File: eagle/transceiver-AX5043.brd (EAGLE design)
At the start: 40 x 35 mm, 43 parts, among them J1 142-0701-851, J2 142-0701-851, J3 142-0701-851, U1 U-ONSEMI-AX5043, U2 LP2985XX-N, X1 TAITIEN-TY

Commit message: Update layout AX5043
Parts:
- R7: device oresat-rcl:.0603-B-NOSILK -> oresat-rcl:.0603-C-NOSILK
- moved D1 63.5 mm to (4.50, 23.9), turned to 90 degrees
- moved C15 50.9 mm to (23.2, 19.3)
- moved C13 50.3 mm to (23.2, 17.1)
- moved C10 49.7 mm to (17.1, 21.9), turned to 270 degrees
- moved C14 48.1 mm to (23.2, 18.2)
- moved C16 45.3 mm to (12.1, 25.4), turned to 90 degrees
- moved C11 41.4 mm to (17.1, 24.1), turned to 90 degrees
- moved R6 39.7 mm to (6.10, 23.9), turned to 270 degrees
- moved C17 39.2 mm to (17.1, 26.8), turned to 270 degrees
- moved C12 35.4 mm to (18.2, 24.1), turned to 90 degrees
- moved R7 30.6 mm to (14.9, 29.0)
- moved JP3 8.47 mm to (31.5, 20.8)
- moved R9 6.31 mm to (19.9, 20.8)
- moved C9 5.80 mm to (12.9, 21.9), turned to 270 degrees
- moved R8 4.45 mm to (21.6, 20.8), turned to 180 degrees
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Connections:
- net N$14: now also JP3.2; no longer JP3.1
- net N$15: now also JP3.1; no longer JP3.2
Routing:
- net 2V7: track 0.00 -> 35.6 mm, vias 0 -> 7
- net N$4: track 0.00 -> 21.3 mm
- net GND: track 2.03 -> 20.4 mm, vias 0 -> 205
- net N$14: track 0.00 -> 17.2 mm, vias 0 -> 1
- net N$5: track 0.00 -> 17.0 mm
- net N$9: track 0.00 -> 16.5 mm
- net N$10: track 0.00 -> 15.8 mm
- net N$7: track 0.00 -> 15.5 mm
- net N$23: track 0.00 -> 15.3 mm
- net N$11: track 0.00 -> 15.0 mm
- net N$8: track 0.00 -> 14.9 mm
- net N$13: track 0.00 -> 14.9 mm
- net N$15: track 0.00 -> 14.2 mm, vias 0 -> 1
- net N$12: track 0.00 -> 14.1 mm
- net 1V8: track 0.00 -> 7.45 mm, vias 0 -> 2
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- added copper zone on layer 1, net 1V8
- added copper zone on layer 1, net 2V7
- added copper zone on layer 1, net N$2
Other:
- outline, holes or cut-outs redrawn

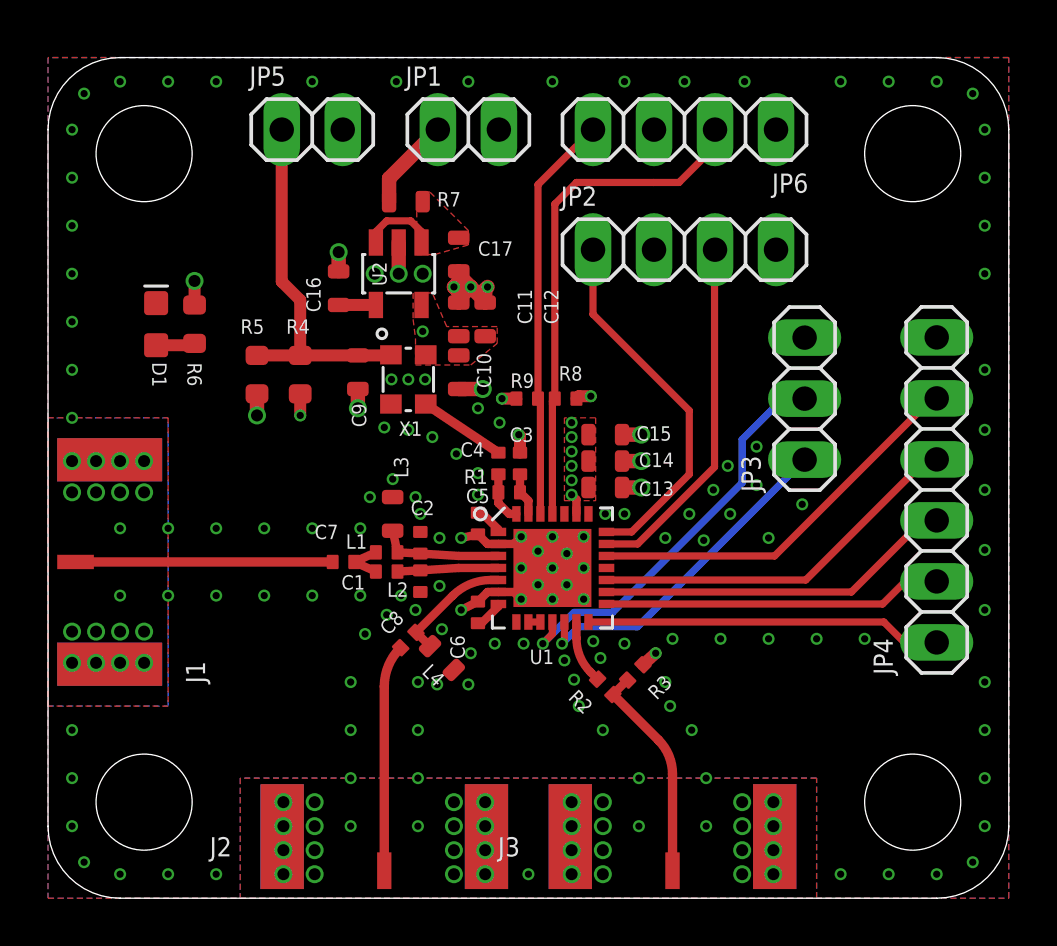
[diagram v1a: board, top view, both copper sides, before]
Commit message: Finalized AX5043 layout
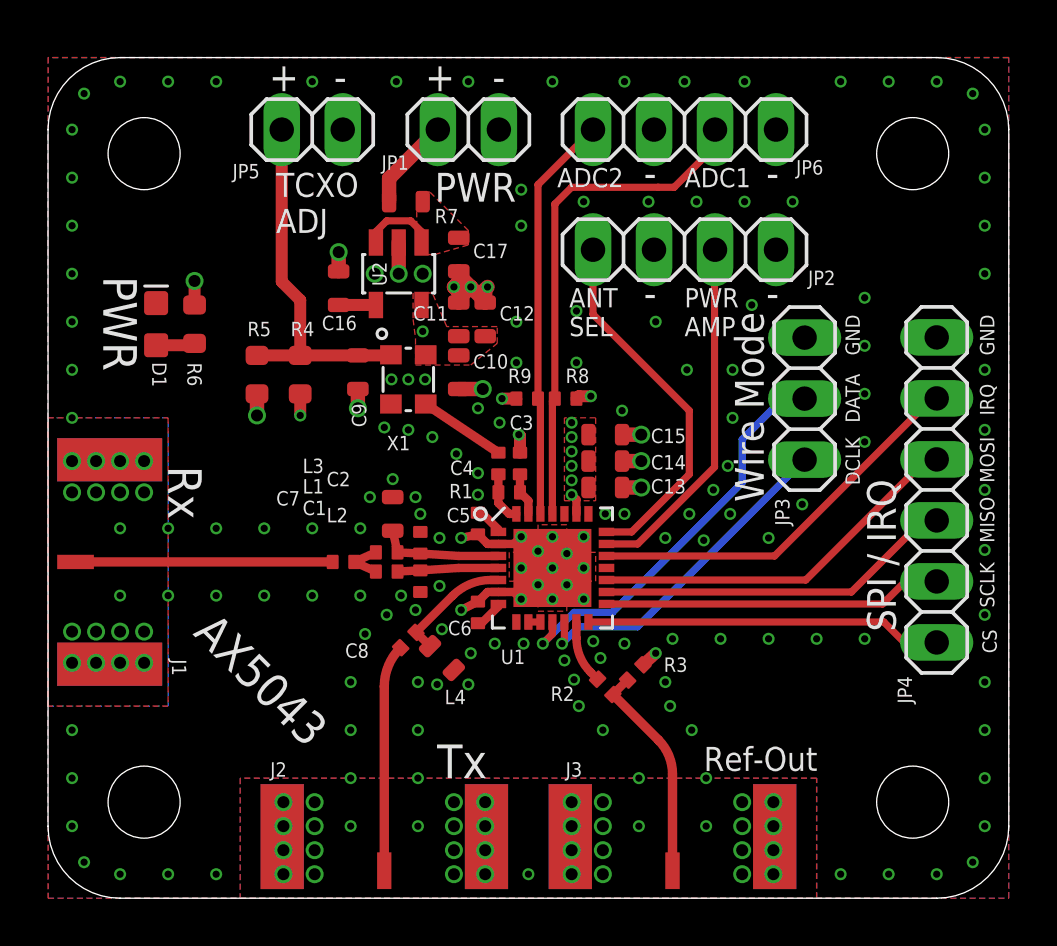
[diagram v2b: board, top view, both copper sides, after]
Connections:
- net N$10 renamed MOSI
- net N$11 renamed MISO
- net N$12 renamed SCLK
- net N$13 renamed CS
- net N$14 renamed DATA
- net N$15 renamed DCLK
- net N$4 renamed ADC1
- net N$5 renamed ADC2
- net N$7 renamed ANTSEL
- net N$8 renamed PWRAMP
- net N$9 renamed IRQ
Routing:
- net GND: vias 205 -> 224
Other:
- board text added: "+"
- board text added: "-"
- board text added: "400 - 525 MHz 800 - 1050 MHz"
- board text added: "ADC1"
- board text added: "ADC2"
- board text added: "ANT SEL"
- board text added: "AX5043"
- board text added: "CS"
- board text added: "DATA"
- board text added: "DCLK"
- board text added: "GND"
- board text added: "IRQ"
- board text added: "MISO"
- board text added: "MOSI"
- board text added: "PWR"
- board text added: "PWR AMP"
- board text added: "Ref-Out"
- board text added: "Rx"
- board text added: "SCLK"
- board text added: "SPI / IRQ"
- board text added: "TCXO ADJ"
- board text added: "Transceiver - AX5043 PSAS / OreSat 2019-10-18 v1.0 E.M. KJ7AOG"
- board text added: "Tx"
- board text added: "Wire Mode"

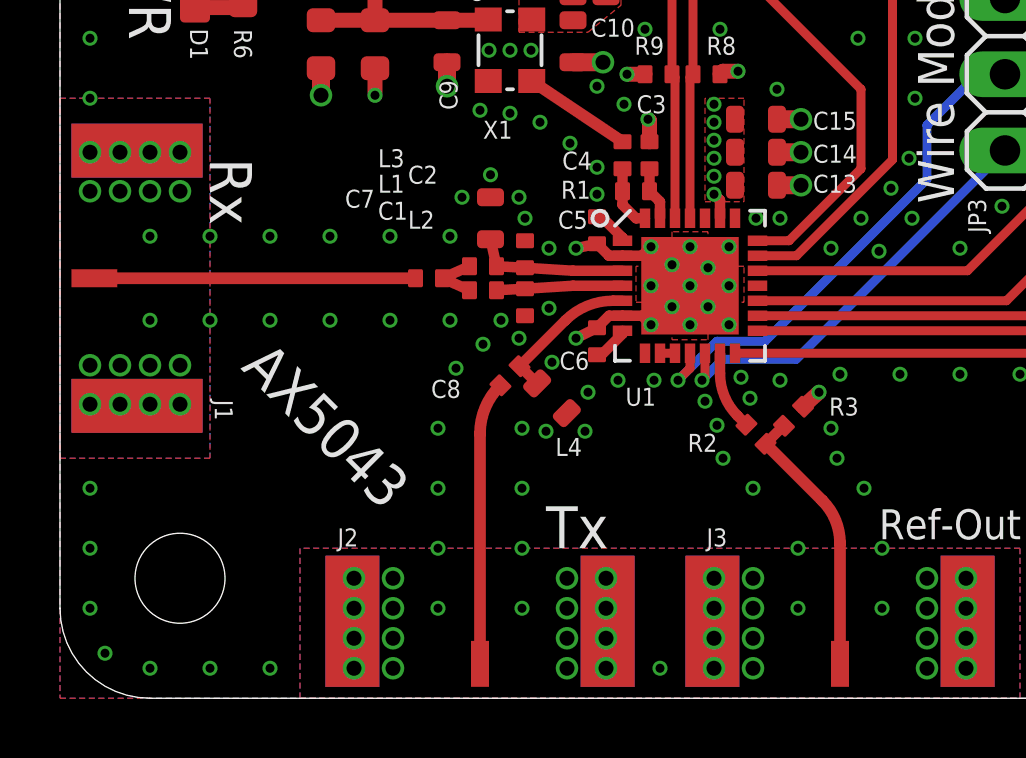
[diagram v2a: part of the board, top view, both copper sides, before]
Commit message: Update AX5043
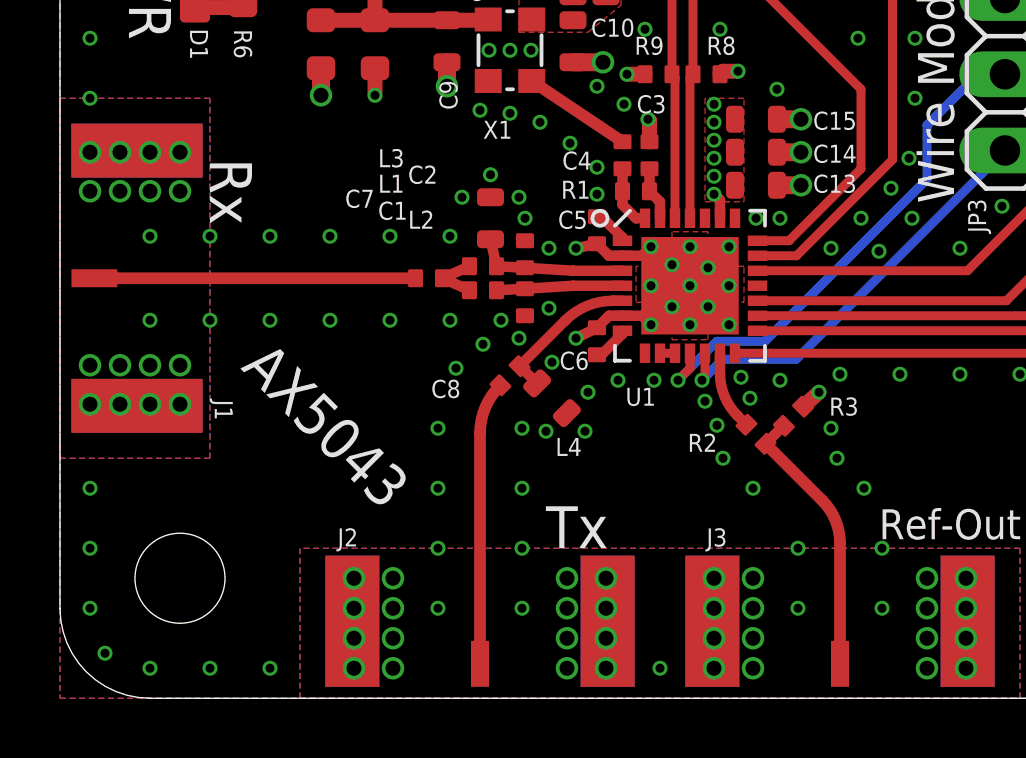
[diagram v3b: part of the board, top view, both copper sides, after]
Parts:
- C5, C6: value 100p -> 82p
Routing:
- added copper zone on layer 1, net REF-OUT
- added copper zone on layer 1, net RX
- added copper zone on layer 1, net TX
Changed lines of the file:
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@@
 <?xml version="1.0" encoding="utf-8"?>
 <!DOCTYPE eagle SYSTEM "eagle.dtd">
-<eagle version="9.2.2">
+<eagle version="9.5.1">
 <drawing>
 <settings>
-<setting alwaysvectorfont="yes"/>
+<setting alwaysvectorfont="no"/>
 <setting verticaltext="up"/>
 </settings>
@@
 <attribute name="NAME" x="18.75" y="18.1" size="0.2" layer="33" ratio="15" rot="R90" align="center"/>
 </element>
-<element name="C5" library="oresat-rcl" package=".0402-C-NOSILK" value="100p" x="17.9" y="15.6" smashed="yes" rot="R270">
+<element name="C5" library="oresat-rcl" package=".0402-C-NOSILK" value="82p" x="17.9" y="15.6" smashed="yes" rot="R270">
 <attribute name="NAME" x="16.6" y="15.65" size="0.6" layer="25" font="vector" ratio="15"/>
 <attribute name="NAME" x="17.9" y="15.6" size="0.2" layer="33" ratio="15" rot="R270" align="center"/>
 </element>
-<element name="C6" library="oresat-rcl" package=".0402-C-NOSILK" value="100p" x="17.9" y="11.9" smashed="yes" rot="R270">
+<element name="C6" library="oresat-rcl" package=".0402-C-NOSILK" value="82p" x="17.9" y="11.9" smashed="yes" rot="R270">
 <attribute name="NAME" x="16.65" y="10.95" size="0.6" layer="25" font="vector" ratio="15"/>
 <attribute name="NAME" x="17.9" y="11.9" size="0.2" layer="33" ratio="15" rot="R270" align="center"/>
@@
 <vertex x="0" y="8"/>
 </polygon>
-<polygon width="0.3" layer="1" thermals="no">
+<polygon width="0.3" layer="1" thermals="no" rank="2">
 <vertex x="8" y="0"/>
 <vertex x="32" y="0"/>
@@
 <wire x1="14.656496875" y1="10.406496875" x2="14" y2="8.821571875" width="0.39" layer="1" curve="45.00009"/>
 <wire x1="14" y1="8.821571875" x2="14" y2="1.146" width="0.39" layer="1"/>
+<polygon width="0.2" layer="1">
+<vertex x="13.8" y="1.7"/>
+<vertex x="13.8" y="1.9"/>
+<vertex x="14" y="2.1"/>
+<vertex x="14.2" y="1.9"/>
+<vertex x="14.2" y="1.7"/>
+</polygon>
 </signal>
 <signal name="RX" class="1">
@@
 <contactref element="C7" pad="1"/>
 <wire x1="1.146" y1="14" x2="11.85" y2="14" width="0.39" layer="1"/>
+<polygon width="0.2" layer="1">
+<vertex x="1.7" y="14.2"/>
+<vertex x="1.9" y="14.2"/>
+<vertex x="2.1" y="14"/>
+<vertex x="1.9" y="13.8"/>
+<vertex x="1.7" y="13.8"/>
+</polygon>
 </signal>
 <signal name="REF-OUT" class="1">
@@
 <wire x1="25.4142125" y1="6.585784375" x2="26" y2="5.17156875" width="0.39" layer="1" curve="-45.00009"/>
 <wire x1="26" y1="5.17156875" x2="26" y2="1.146" width="0.39" layer="1"/>
+<polygon width="0.2" layer="1">
+<vertex x="25.8" y="1.7"/>
+<vertex x="25.8" y="1.9"/>
+<vertex x="26" y="2.1"/>
+<vertex x="26.2" y="1.9"/>
+<vertex x="26.2" y="1.7"/>
+</polygon>
 </signal>
 <signal name="N$23">
@@
 <contactref element="R6" pad="1"/>
 <contactref element="R7" pad="1"/>
-<wire x1="22.5" y1="17" x2="22.5" y2="17.1" width="0.35" layer="1"/>
 <via x="21.8" y="16.8" extent="1-16" drill="0.3"/>
 <via x="21.8" y="17.4" extent="1-16" drill="0.3"/>

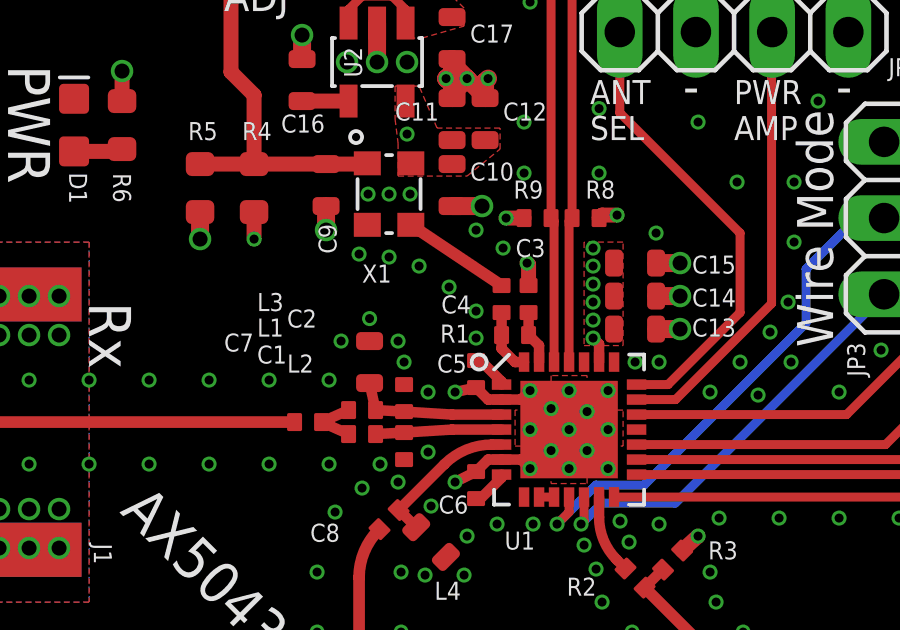
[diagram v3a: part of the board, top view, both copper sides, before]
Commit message: AX5043 layout move mark
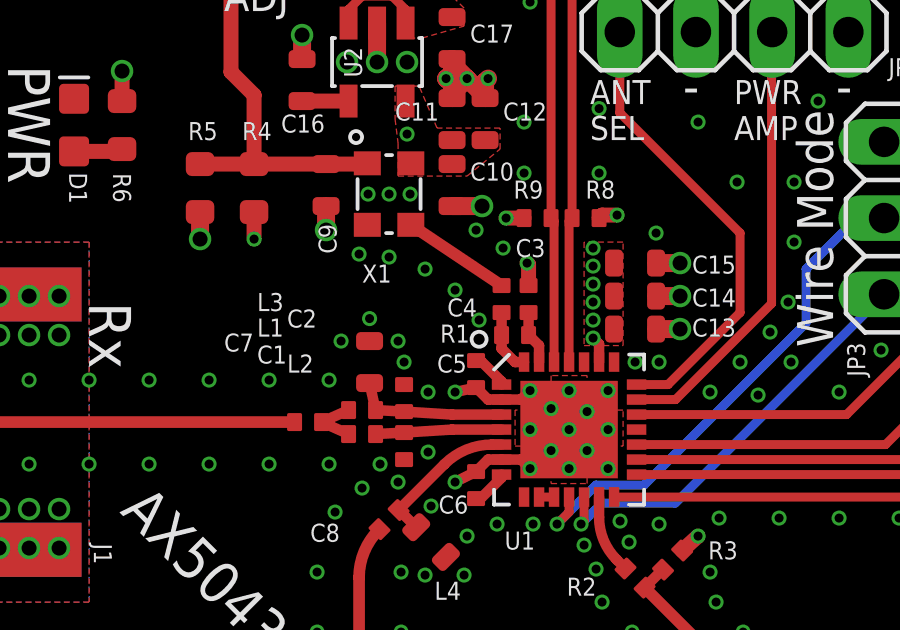
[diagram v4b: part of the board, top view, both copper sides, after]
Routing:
- net GND: vias 224 -> 223
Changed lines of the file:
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@@
 </element>
 <element name="C4" library="oresat-rcl" package=".0402-C-NOSILK" value="1n" x="18.75" y="18.1" smashed="yes" rot="R90">
-<attribute name="NAME" x="16.74" y="17.62" size="0.6" layer="25" font="vector" ratio="15"/>
+<attribute name="NAME" x="16.94" y="17.52" size="0.6" layer="25" font="vector" ratio="15"/>
 <attribute name="NAME" x="18.75" y="18.1" size="0.2" layer="33" ratio="15" rot="R90" align="center"/>
 </element>
@@
 <via x="15" y="19.5" extent="1-16" drill="0.3"/>
 <via x="14" y="19.6" extent="1-16" drill="0.3"/>
-<via x="16" y="19.2" extent="1-16" drill="0.3"/>
-<via x="17" y="18.5" extent="1-16" drill="0.3"/>
-<via x="17.9" y="17.7" extent="1-16" drill="0.3"/>
-<via x="17.9" y="16.8" extent="1-16" drill="0.3"/>
+<via x="16.2" y="19.1" extent="1-16" drill="0.3"/>
+<via x="17.2" y="18.4" extent="1-16" drill="0.3"/>
+<via x="18" y="17.4" extent="1-16" drill="0.3"/>
 <via x="17.9" y="20.4" extent="1-16" drill="0.3"/>
 <via x="18.8" y="19.8" extent="1-16" drill="0.3"/>
